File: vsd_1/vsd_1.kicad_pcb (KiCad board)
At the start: 2 copper layers, 90 x 120 mm, 4 parts, among them U1 CAMERA-OV7670

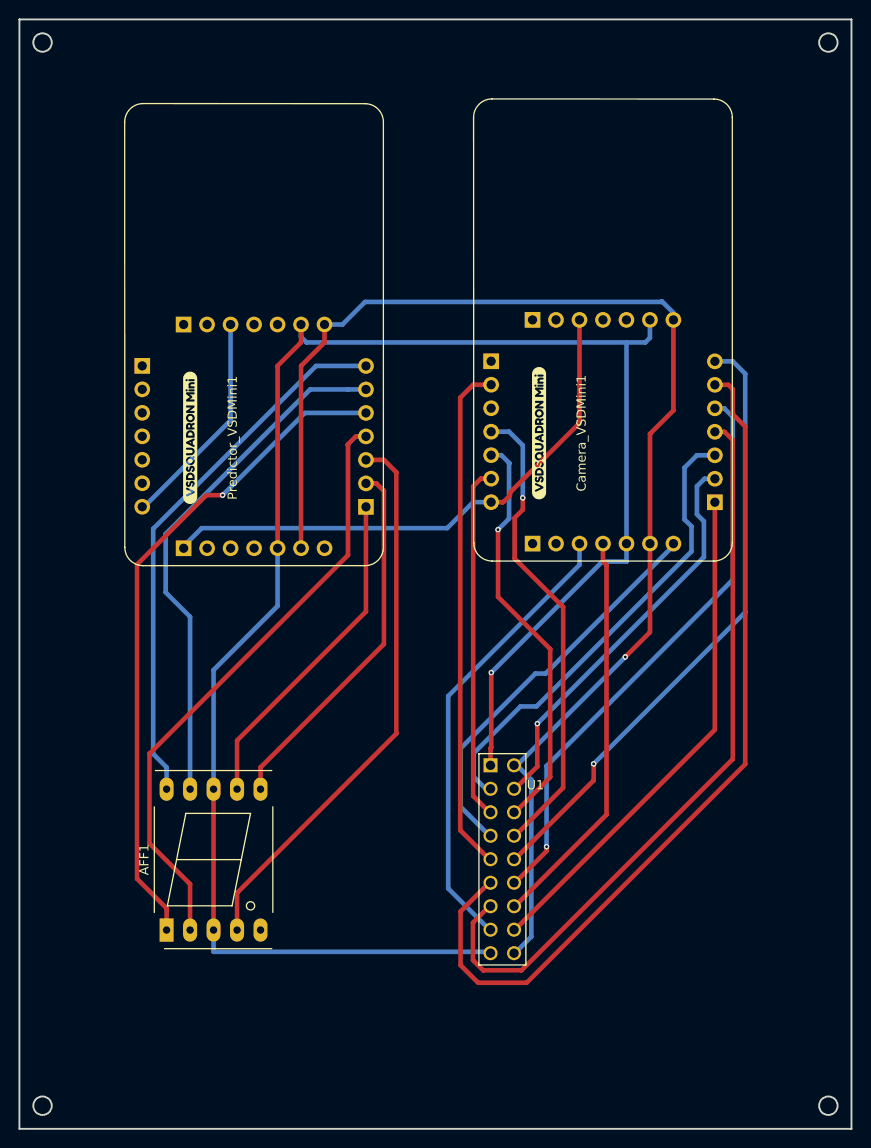
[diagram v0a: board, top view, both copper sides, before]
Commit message: added copper pour, and resolved issues introduced
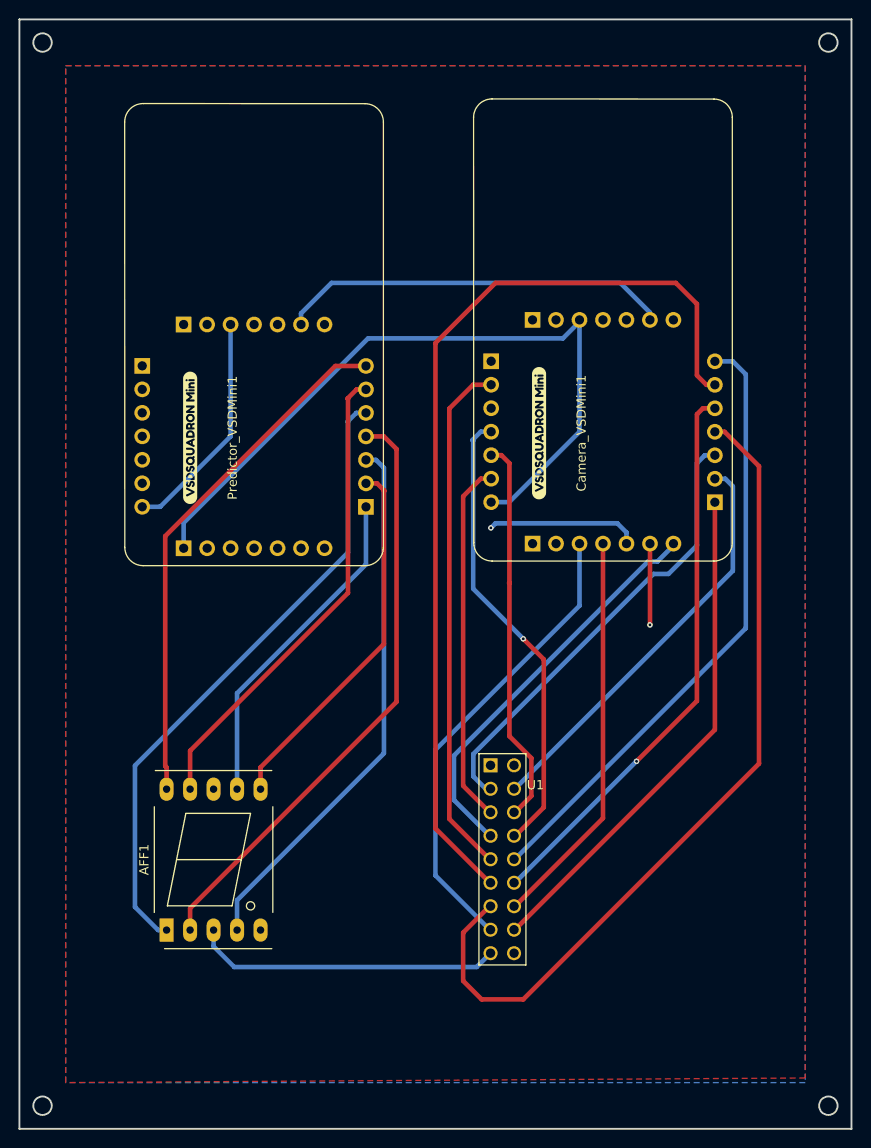
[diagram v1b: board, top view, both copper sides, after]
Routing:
- net GND: track 142.6 -> 8.80 mm
- net +3.3V: track 196.6 -> 92.2 mm
- net Net-(Camera_VSDMini1-Nano_PD5): track 59.9 -> 79.6 mm
- net Net-(Camera_VSDMini1-Nano_PC3): track 81.5 -> 91.2 mm
- net Net-(Camera_VSDMini1-Nano_PC5): track 95.0 -> 102.9 mm
- net Net-(AFF1-f): track 56.8 -> 51.7 mm
- net Net-(AFF1-e): track 72.4 -> 68.9 mm, vias 1 -> 0
- net Net-(Camera_VSDMini1-Nano_PD3): track 44.6 -> 41.9 mm, vias 1 -> 0
- net Net-(AFF1-g): track 59.1 -> 56.8 mm
- net Net-(AFF1-c): track 60.5 -> 58.9 mm
- net Net-(Camera_VSDMini1-Nano_PC4): track 62.6 -> 61.1 mm
- net Net-(Camera_VSDMini1-Nano_PD2): track 51.1 -> 49.8 mm
- net Net-(Camera_VSDMini1-Nano_PC2): track 50.7 -> 49.6 mm
- net Net-(Camera_VSDMini1-Nano_PA1): track 49.6 -> 50.7 mm
- net Net-(Predictor_VSDMini1-Nano_PD5): track 23.8 -> 24.8 mm
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- added copper zone on F.Cu, net +3.3V
- added copper zone on B.Cu, net GND
